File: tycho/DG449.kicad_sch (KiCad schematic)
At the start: 1 part, among them U14 DG449

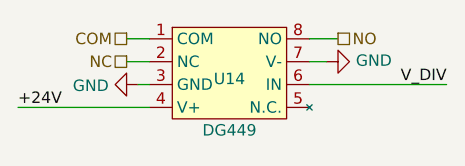
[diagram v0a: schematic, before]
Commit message: ERC cleanup put everything on 0.05mm grid
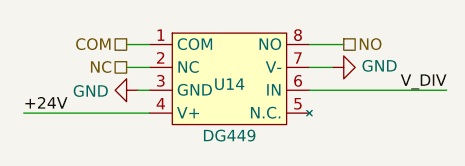
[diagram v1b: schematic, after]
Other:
- moved on the sheet: U14
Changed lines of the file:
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@@
 (kicad_sch (version 20230121) (generator eeschema)
   (paper "A4")
-  (wire (pts (xy 143.51 108.585) (xy 144.78 108.585))
+  (wire (pts (xy 143.51 109.22) (xy 144.78 109.22))
     (stroke (width 0) (type default))
   )
-  (wire (pts (xy 177.8 108.585) (xy 162.56 108.585))
+  (wire (pts (xy 177.8 109.22) (xy 162.56 109.22))
     (stroke (width 0) (type default))
   )
-  (wire (pts (xy 142.24 106.045) (xy 144.78 106.045))
+  (wire (pts (xy 142.24 106.68) (xy 144.78 106.68))
     (stroke (width 0) (type default))
   )
-  (wire (pts (xy 162.56 103.505) (xy 165.735 103.505))
+  (wire (pts (xy 162.56 104.14) (xy 166.37 104.14))
     (stroke (width 0) (type default))
   )
-  (wire (pts (xy 142.24 103.505) (xy 144.78 103.505))
+  (wire (pts (xy 142.24 104.14) (xy 144.78 104.14))
     (stroke (width 0) (type default))
   )
-  (wire (pts (xy 130.175 111.125) (xy 144.78 111.125))
+  (wire (pts (xy 130.81 111.76) (xy 144.78 111.76))
     (stroke (width 0) (type default))
   )
-  (wire (pts (xy 162.56 106.045) (xy 164.465 106.045))
+  (wire (pts (xy 162.56 106.68) (xy 165.1 106.68))
     (stroke (width 0) (type default))
   )
-  (label "+24V" (at 130.175 111.125 0) (fields_autoplaced)
+  (label "+24V" (at 130.81 111.76 0) (fields_autoplaced)
     (effects (font (size 1.27 1.27)) (justify left bottom))
   )
-  (label "V_DIV" (at 177.8 108.585 180) (fields_autoplaced)
+  (label "V_DIV" (at 177.8 109.22 180) (fields_autoplaced)
     (effects (font (size 1.27 1.27)) (justify right bottom))
   )
-  (hierarchical_label "NO" (shape passive) (at 165.735 103.505 0) (fields_autoplaced)
+  (hierarchical_label "NO" (shape passive) (at 166.37 104.14 0) (fields_autoplaced)
     (effects (font (size 1.27 1.27)) (justify left))
   )
-  (hierarchical_label "COM" (shape passive) (at 142.24 103.505 180) (fields_autoplaced)
+  (hierarchical_label "COM" (shape passive) (at 142.24 104.14 180) (fields_autoplaced)
     (effects (font (size 1.27 1.27)) (justify right))
   )
-  (hierarchical_label "NC" (shape passive) (at 142.24 106.045 180) (fields_autoplaced)
+  (hierarchical_label "NC" (shape passive) (at 142.24 106.68 180) (fields_autoplaced)
     (effects (font (size 1.27 1.27)) (justify right))
   )
-  (symbol (lib_id "power:GND") (at 164.465 106.045 90) (unit 1)
+  (symbol (lib_id "power:GND") (at 165.1 106.68 90) (unit 1)
     (in_bom yes) (on_board yes) (dnp no)
-    (property "Reference" "#PWR059" (at 170.815 106.045 0)
+    (property "Reference" "#PWR059" (at 171.45 106.68 0)
       (effects (font (size 1.27 1.27)) hide)
     )
-    (property "Value" "GND" (at 167.7162 105.918 90)
+    (property "Value" "GND" (at 168.3512 106.553 90)
       (effects (font (size 1.27 1.27)) (justify right))
     )
-    (property "Footprint" "" (at 164.465 106.045 0)
+    (property "Footprint" "" (at 165.1 106.68 0)
       (effects (font (size 1.27 1.27)) hide)
     )
-    (property "Datasheet" "" (at 164.465 106.045 0)
+    (property "Datasheet" "" (at 165.1 106.68 0)
       (effects (font (size 1.27 1.27)) hide)
     )
@@
     )
   )
-  (symbol (lib_id "tycho:DG449") (at 153.67 107.315 0) (unit 1)
+  (symbol (lib_id "tycho:DG449") (at 153.67 107.95 0) (unit 1)
     (in_bom yes) (on_board yes) (dnp no)
-    (property "Reference" "U14" (at 153.67 107.95 0)
+    (property "Reference" "U14" (at 153.67 108.585 0)
       (effects (font (size 1.27 1.27)))
     )
-    (property "Value" "DG449" (at 153.67 113.665 0)
+    (property "Value" "DG449" (at 153.67 114.3 0)
       (effects (font (size 1.27 1.27)))
     )
-    (property "Footprint" "Package_TO_SOT_SMD:SOT-23-8_Handsoldering" (at 153.67 107.315 0)
+    (property "Footprint" "Package_TO_SOT_SMD:SOT-23-8_Handsoldering" (at 153.67 107.95 0)
       (effects (font (size 1.27 1.27)) hide)
     )
-    (property "Datasheet" "https://www.vishay.com/docs/73897/dg449.pdf" (at 153.67 107.315 0)
+    (property "Datasheet" "https://www.vishay.com/docs/73897/dg449.pdf" (at 153.67 107.95 0)
       (effects (font (size 1.27 1.27)) hide)
     )
-    (property "Manufacturer" "Vishay Siliconix" (at 153.67 107.315 0)
+    (property "Manufacturer" "Vishay Siliconix" (at 153.67 107.95 0)
       (effects (font (size 1.27 1.27)) hide)
     )
-    (property "Part Number" "DG449DS-T1-E3" (at 153.67 107.315 0)
+    (property "Part Number" "DG449DS-T1-E3" (at 153.67 107.95 0)
       (effects (font (size 1.27 1.27)) hide)
     )
-    (property "Description" "IC SWITCH SPDT X 1 45OHM SOT23-8" (at 153.67 107.315 0)
+    (property "Description" "IC SWITCH SPDT X 1 45OHM SOT23-8" (at 153.67 107.95 0)
       (effects (font (size 1.27 1.27)) hide)
     )
@@
     )
   )
-  (symbol (lib_id "power:GND") (at 143.51 108.585 270) (unit 1)
+  (symbol (lib_id "power:GND") (at 143.51 109.22 270) (unit 1)
     (in_bom yes) (on_board yes) (dnp no)
-    (property "Reference" "#PWR039" (at 137.16 108.585 0)
+    (property "Reference" "#PWR039" (at 137.16 109.22 0)
       (effects (font (size 1.27 1.27)) hide)
     )
-    (property "Value" "GND" (at 140.2588 108.712 90)
+    (property "Value" "GND" (at 140.2588 109.347 90)
       (effects (font (size 1.27 1.27)) (justify right))
     )
-    (property "Footprint" "" (at 143.51 108.585 0)
+    (property "Footprint" "" (at 143.51 109.22 0)
       (effects (font (size 1.27 1.27)) hide)
     )
-    (property "Datasheet" "" (at 143.51 108.585 0)
+    (property "Datasheet" "" (at 143.51 109.22 0)
       (effects (font (size 1.27 1.27)) hide)
     )

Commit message: Fix some ERC errors
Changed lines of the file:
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@@
     (stroke (width 0) (type default))
   )
-  (wire (pts (xy 177.8 109.22) (xy 162.56 109.22))
+  (wire (pts (xy 162.56 109.22) (xy 177.8 109.22))
     (stroke (width 0) (type default))
   )
